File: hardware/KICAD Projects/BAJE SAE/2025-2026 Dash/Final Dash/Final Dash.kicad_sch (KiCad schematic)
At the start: 17 parts, among them IC1 MAX6955ATL+, IC2 MAX6955ATL+, J1 TO DEUTSCH CONNECTOR, J12 Conn_01x02, J2 Servo 1 (Tach), J3 Servo 2 (Speed), J4 Servo 3 (Fuel), U1 XIAO-ESP32-S3-SMD, U2 MCP25625x-x-ML, U3 EA_DOGM128X-6, Y1 Crystal

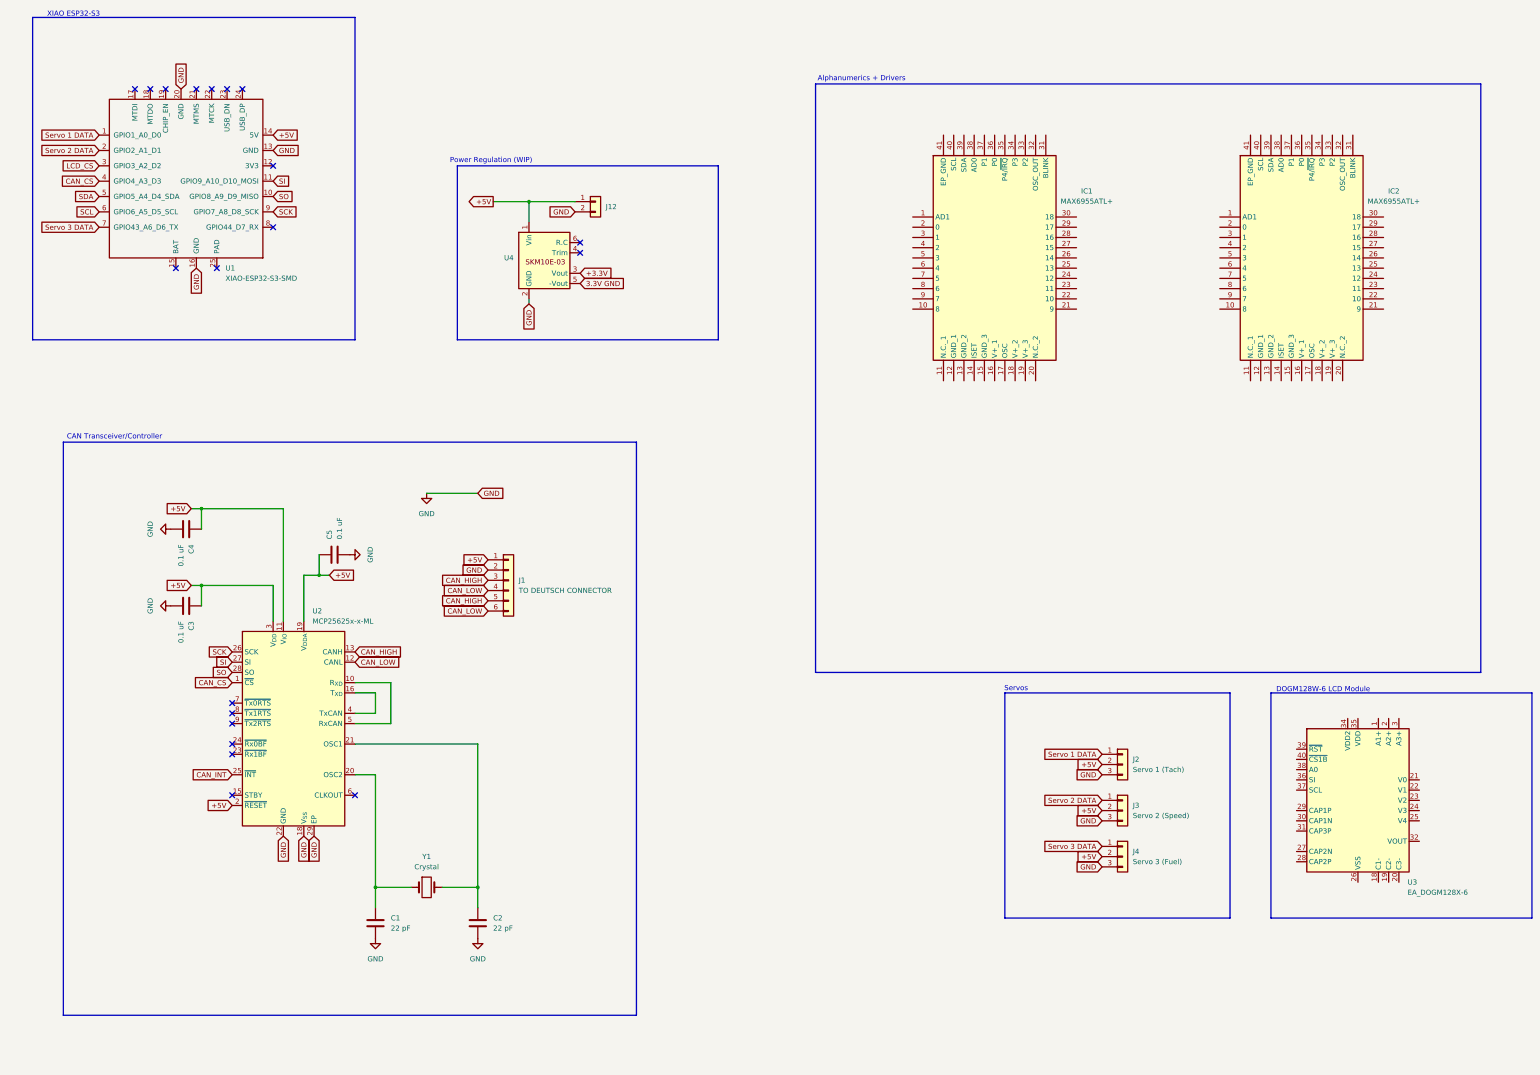
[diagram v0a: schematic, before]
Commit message: Updating Final Dash setup
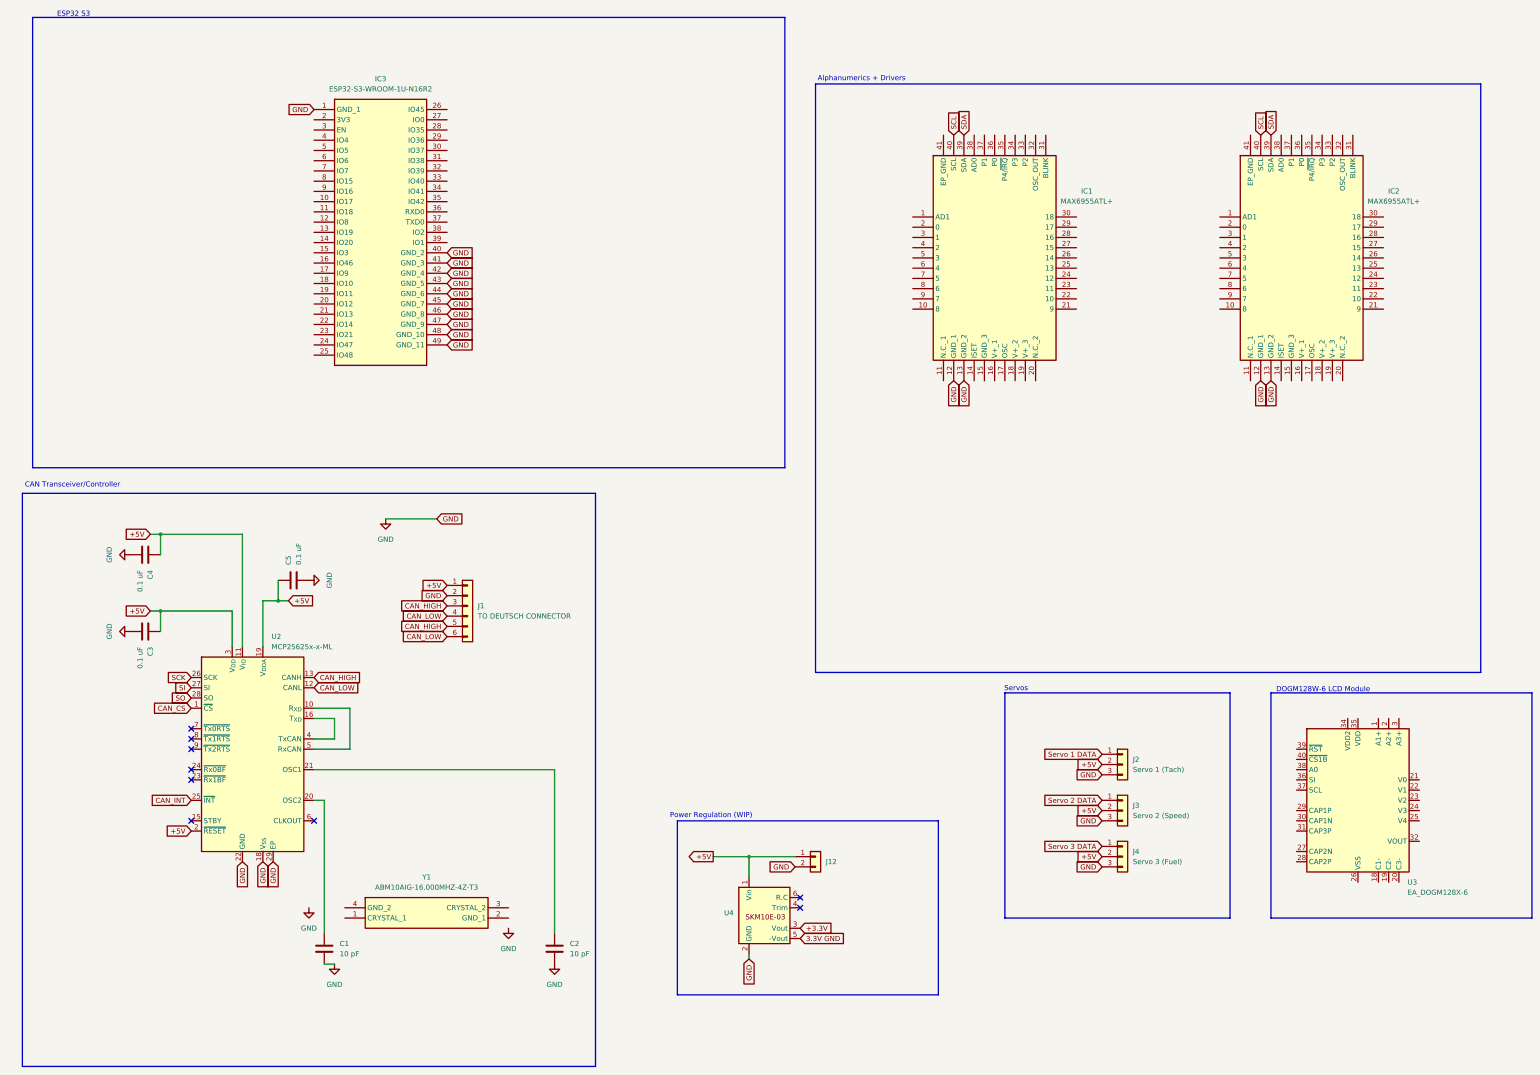
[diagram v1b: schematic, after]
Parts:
- removed U1: XIAO-ESP32-S3-SMD, symbol Seeed_Studio_XIAO_Series:XIAO-ESP32-S3-SMD
- removed Y1: Crystal, symbol Device:Crystal
- added IC3: ESP32-S3-WROOM-1U-N16R2, ESP32-S3-WROOM-1U-N16R2:ESP32S3WROOM1UN16R2, symbol ESP32-S3-WROOM-1U-N16R2:ESP32-S3-WROOM-1U-N16R2
- added Y1: ABM10AIG-16.000MHZ-4Z-T3, ABM10AIG16000MHZ4ZT3, symbol ABM10AIG-16_000MHZ-4Z-T3:ABM10AIG-16.000MHZ-4Z-T3
- C1, C2: value 22 pF -> 10 pF
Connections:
- net GND: now also IC1.12 (GND_1), IC1.13 (GND_2), IC2.12 (GND_1), IC2.13 (GND_2), IC3.1 (GND_1), IC3.40 (GND_2), IC3.41 (GND_3), IC3.42 (GND_4), IC3.43 (GND_5), IC3.44 (GND_6), IC3.45 (GND_7), IC3.46 (GND_8), IC3.47 (GND_9), IC3.48 (GND_10), IC3.49 (GND_11)
- net SCL: now also IC1.40 (SCL), IC2.40 (SCL)
- net SDA: now also IC1.39 (SDA), IC2.39 (SDA)
- no-connect marks 20 -> 9
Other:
- note added: "ESP32 S3"
- note removed: "XIAO ESP32-S3"
- moved on the sheet: C1, C2, C3, C4, C5, J1, J12, U2, U4
